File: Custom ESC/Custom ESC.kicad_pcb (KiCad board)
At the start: 4 copper layers, 83.2 x 50.4 mm, 104 parts, among them J1 XT60-F, J2 Conn_ARM_SWD_TagConnect_TC203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, J3 MOTOR_A, J4 MOTOR_B, J5 MOTOR_C, Q1 NMOS, Q2 NMOS, Q3 NMOS, Q4 NMOS, Q5 NMOS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

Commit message: fixed some stuff
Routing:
- net GND: track 50.5 -> 51.7 mm, vias 5 -> 6
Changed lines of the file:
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@@
+	)
+	(via
+		(at 120.7 109.3)
+		(size 0.6)
+		(drill 0.3)
+		(layers "F.Cu" "B.Cu")
+		(net 1)
 	)
 	(via
@@
 	)
 	(segment
+		(start 121.575 107.5375)
+		(end 121.9125 107.875)
+		(width 0.2)
+		(layer "B.Cu")
+		(net 1)
+	)
+	(segment
 		(start 136.6525 93.4775)
 		(end 135.85 92.675)
@@
 	)
 	(segment
-		(start 121.575 108.9625)
+		(start 120.7 109.3)
 		(end 121.9125 109.3)
-		(width 0.5)
+		(width 0.2)
 		(layer "B.Cu")
 		(net 1)
@@
 	)
 	(segment
-		(start 121.575 107.5375)
-		(end 121.575 108.9625)
-		(width 0.5)
-		(layer "B.Cu")
-		(net 1)
-	)
-	(segment
 		(start 134.9075 87.3975)
 		(end 136.625 87.3975)
@@
 	)
 	(segment
+		(start 121.9125 107.875)
+		(end 121.9125 109.3)
+		(width 0.2)
+		(layer "B.Cu")
+		(net 1)
+	)
+	(segment
 		(start 145.350943 96.275)
 		(end 144.400943 95.325)
@@
 	)
 	(segment
+		(start 119.175 107.5375)
+		(end 121.575 107.5375)
+		(width 0.2)
+		(layer "B.Cu")
+		(net 1)
+	)
+	(segment
 		(start 152.140176 108.424)
 		(end 153.6865 108.424)
@@
 		(layer "B.Cu")
 		(net 1)
-	)
-	(segment
-		(start 119.175 107.5375)
-		(end 121.575 107.5375)
-		(width 0.5)
-		(layer "B.Cu")
-		(net 1)

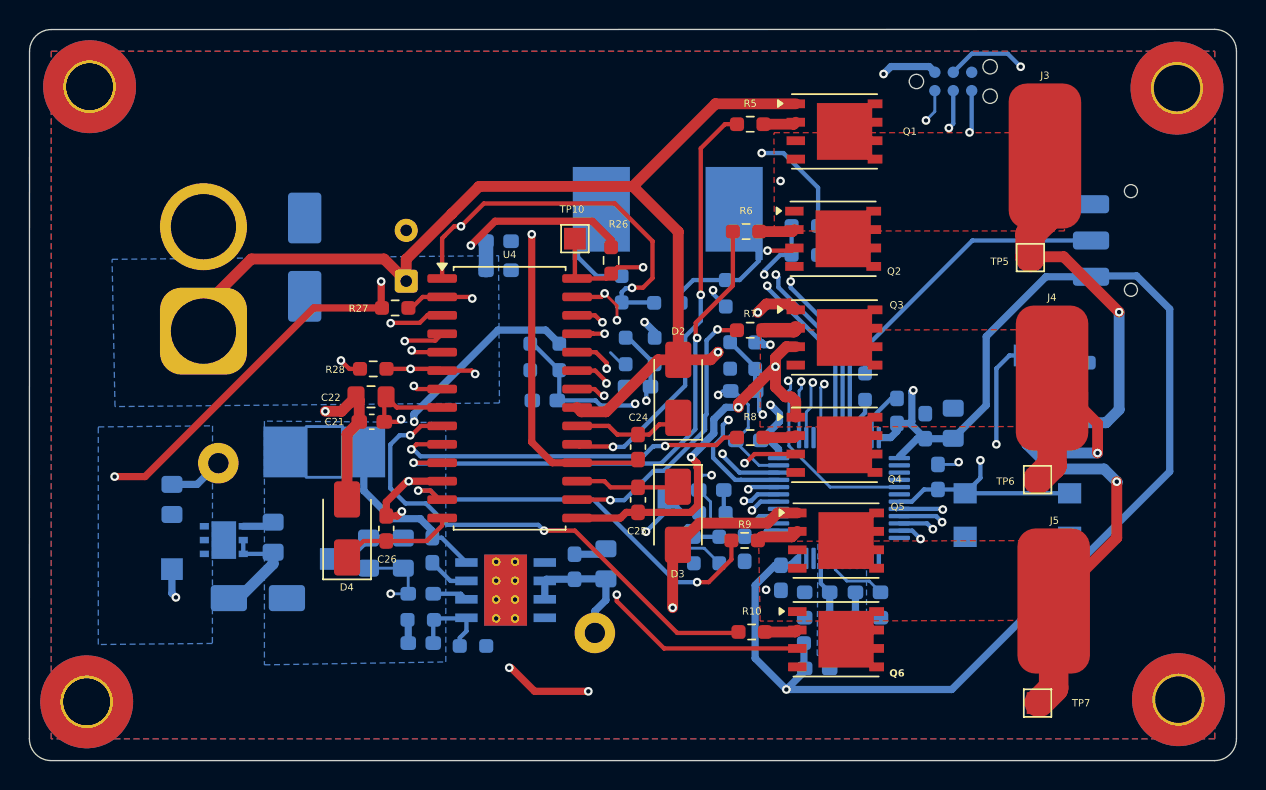
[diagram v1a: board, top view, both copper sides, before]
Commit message: fixed some DRC stuff, still have some issues
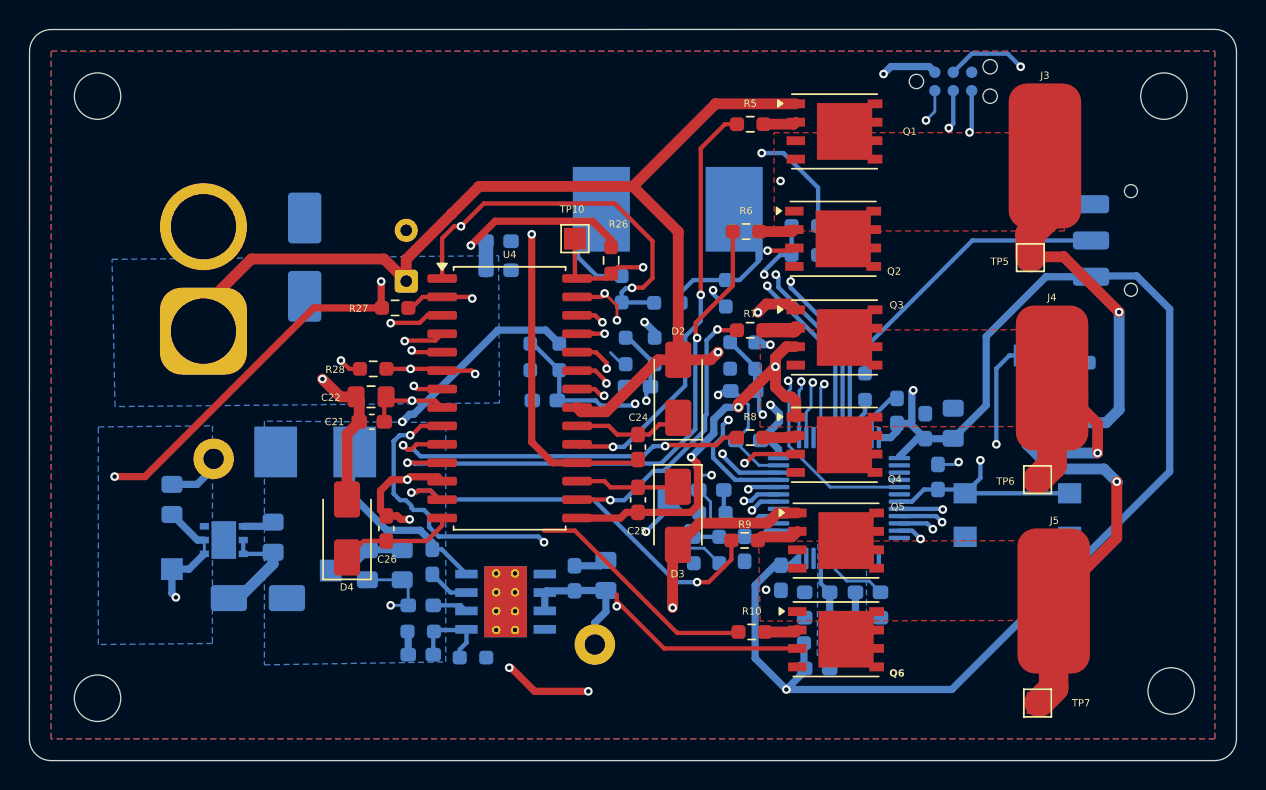
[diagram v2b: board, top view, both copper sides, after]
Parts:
- removed the   at (99.8, 116.8)
- removed the   at (175.0, 116.6)
- removed the   at (174.9, 74.5)
- removed the   at (100.0, 74.3)
- removed ? (x2): , 
- added  : MountingHole_3.2mm_M3, MountingHole:MountingHole_3.2mm_M3, F.Cu at (100.5, 75.0)
- added  : MountingHole_3.2mm_M3, MountingHole:MountingHole_3.2mm_M3, F.Cu at (100.5, 116.5)
- added  : MountingHole_3.2mm_M3, MountingHole:MountingHole_3.2mm_M3, F.Cu at (174.0, 75.0)
- added  : MountingHole_3.2mm_M3, MountingHole:MountingHole_3.2mm_M3, F.Cu at (174.5, 116.0)
- moved C14 0.80 mm to (121.5, 107.3)
- moved C15 0.80 mm to (119.1, 107.3)
- moved R4 0.80 mm to (122.8, 111.9)
- moved C12 0.80 mm to (135.5, 108.0)
- moved C13 0.80 mm to (133.4, 108.2)
- moved C16 0.80 mm to (123.6, 107.1)
- moved C17 0.80 mm to (122.8, 110.1)
- moved C18 0.80 mm to (122.8, 113.5)
- moved R3 0.80 mm to (126.4, 113.7)
- moved TP1 0.80 mm to (134.8, 112.8)
- moved TP3 0.80 mm to (116.6, 107.7)
- moved U2 0.80 mm to (128.6, 109.8)
- moved L1 0.62 mm to (115.5, 99.5)
- moved TP2 0.44 mm to (108.5, 100.0)
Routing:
- net +3V3: track 281.9 -> 288.5 mm
- net /VS3: track 87.0 -> 89.4 mm
- net Net-(U2-SW): track 12.1 -> 13.8 mm
- net /LO2: track 25.4 -> 26.8 mm
- net /COM: track 121.1 -> 119.8 mm
- net /HO3: track 28.1 -> 29.1 mm
- net VCC: track 172.5 -> 173.5 mm
- net /CAO: track 85.8 -> 86.7 mm
- net /LO3: track 35.3 -> 36.2 mm
- net /LO1: track 37.2 -> 38.0 mm
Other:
- rule pad_to_mask_clearance: 0.1 -> 0
